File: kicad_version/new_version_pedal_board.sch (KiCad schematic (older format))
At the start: 0 parts

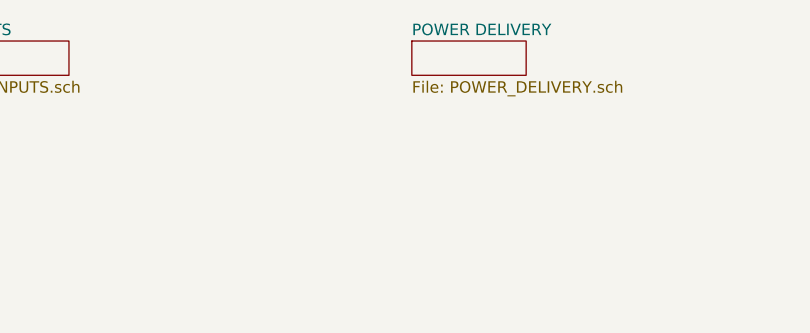
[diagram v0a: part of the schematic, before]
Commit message: Added rev B design and kicad version of rev A
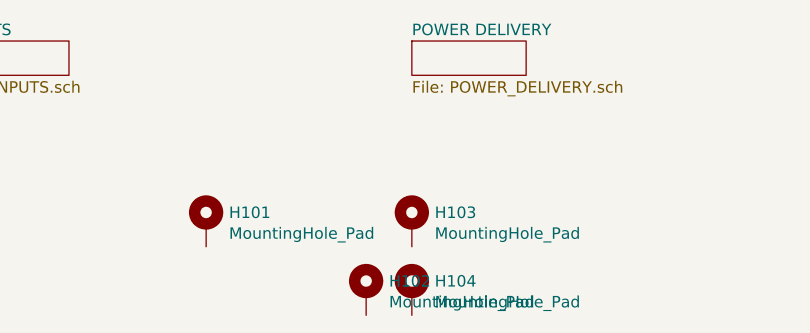
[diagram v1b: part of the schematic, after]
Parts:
- added H101, H102, H103, H104: MountingHole_Pad, MountingHole:MountingHole_3.2mm_M3_DIN965_Pad_TopBottom, symbol Mechanical:MountingHole_Pad
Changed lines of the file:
@@
 F1 "OUTPUTS.sch" 50
 $EndSheet
+$Comp
+L Mechanical:MountingHole_Pad H103
+U 1 1 618FA362
+P 5000 1800
+F 0 "H103" H 5100 1849 50  0000 L CNN
+F 1 "MountingHole_Pad" H 5100 1758 50  0000 L CNN
+F 2 "MountingHole:MountingHole_3.2mm_M3_DIN965_Pad_TopBottom" H 5000 1800 50  0001 C CNN
+F 3 "~" H 5000 1800 50  0001 C CNN
+	1    5000 1800
+	1    0    0    -1
+$EndComp
+$Comp
+L Mechanical:MountingHole_Pad H101
+U 1 1 618FACF2
+P 4100 1800
+F 0 "H101" H 4200 1849 50  0000 L CNN
+F 1 "MountingHole_Pad" H 4200 1758 50  0000 L CNN
+F 2 "MountingHole:MountingHole_3.2mm_M3_DIN965_Pad_TopBottom" H 4100 1800 50  0001 C CNN
+F 3 "~" H 4100 1800 50  0001 C CNN
+	1    4100 1800
+	1    0    0    -1
+$EndComp
+$Comp
+L Mechanical:MountingHole_Pad H104
+U 1 1 618FB9FA
+P 5000 2100
+F 0 "H104" H 5100 2149 50  0000 L CNN
+F 1 "MountingHole_Pad" H 5100 2058 50  0000 L CNN
+F 2 "MountingHole:MountingHole_3.2mm_M3_DIN965_Pad_TopBottom" H 5000 2100 50  0001 C CNN
+F 3 "~" H 5000 2100 50  0001 C CNN
+	1    5000 2100
+	1    0    0    -1
+$EndComp
+$Comp
+L Mechanical:MountingHole_Pad H102
+U 1 1 618FBA00
+P 4800 2100
+F 0 "H102" H 4900 2149 50  0000 L CNN
+F 1 "MountingHole_Pad" H 4900 2058 50  0000 L CNN
+F 2 "MountingHole:MountingHole_3.2mm_M3_DIN965_Pad_TopBottom" H 4800 2100 50  0001 C CNN
+F 3 "~" H 4800 2100 50  0001 C CNN
+	1    4800 2100
+	1    0    0    -1
+$EndComp
 $EndSCHEMATC
